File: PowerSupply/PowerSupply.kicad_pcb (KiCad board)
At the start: 2 copper layers, 34.9 x 22.9 mm, 27 parts, among them IC1 MCP73832T-2DCI_OT, J1 Conn_01x04_Male, J2 Barrel_Jack, Q1 DMP2045U-7, SW1 SW_SPST, U1 AP3012, U2 AP3012

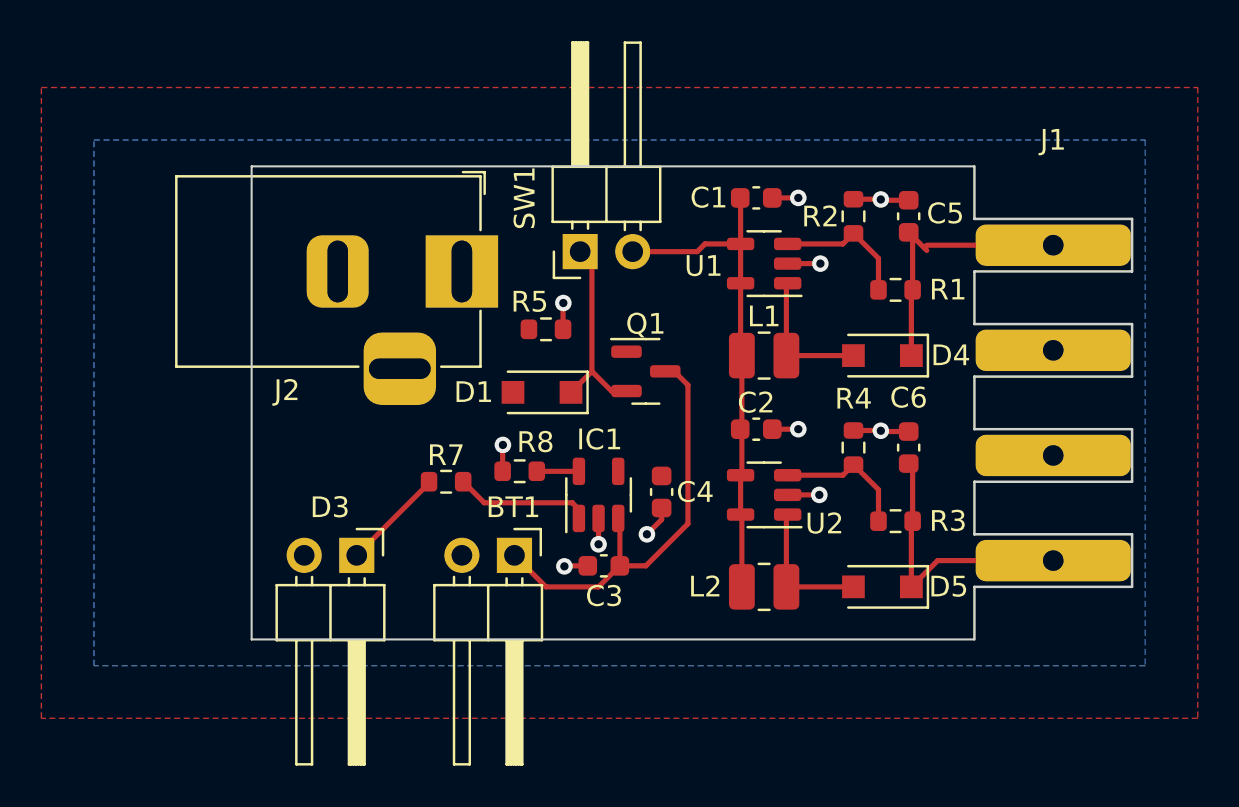
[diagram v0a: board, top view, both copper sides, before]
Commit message: Added silk screen and fabrication files.
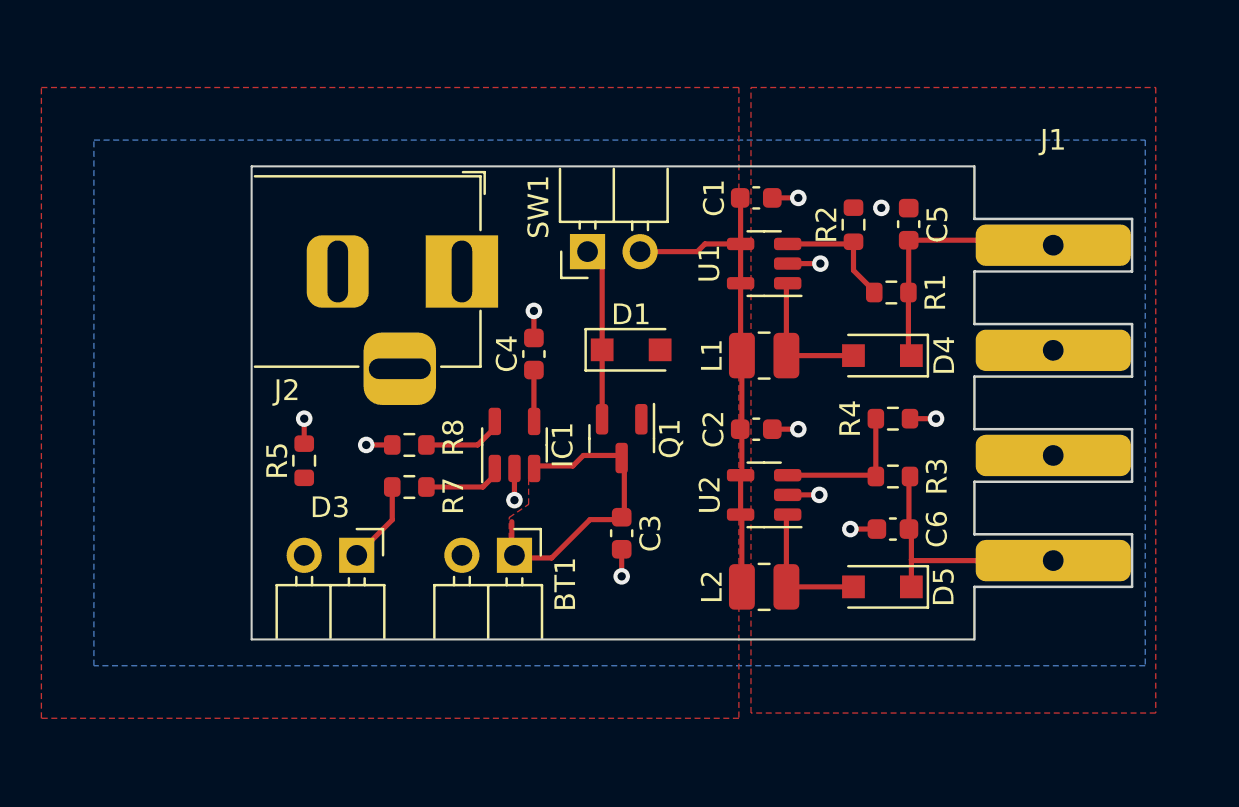
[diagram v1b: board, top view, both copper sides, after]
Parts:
- added REF**: TUNL LOGO small, Library:TUNL LOGO small, B.Cu at (167.0, 75.0)
- D1, D4, D5: value 2SS100L -> NRVB120VLSFT1G
- moved R5 13.3 mm to (142.2, 79.0), turned to 90 degrees
- moved C4 9.09 mm to (153.3, 73.8), turned to 90 degrees
- moved R8 5.48 mm to (147.3, 78.2)
- moved D1 4.77 mm to (158.0, 73.6), turned to 0 degrees
- moved IC1 4.73 mm to (152.4, 78.2)
- moved C6 4.01 mm to (170.7, 82.3), turned to 180 degrees
- moved Q1 3.45 mm to (157.6, 77.9), turned to -90 degrees
- moved R4 2.36 mm to (170.7, 77.0), turned to 0 degrees
- moved R3 2.16 mm to (170.7, 79.8)
- moved R7 1.80 mm to (147.3, 80.3)
- moved C3 1.80 mm to (157.6, 82.5), turned to 90 degrees
- moved R2 0.41 mm to (168.8, 67.6)
- moved C5 0.38 mm to (171.4, 67.6)
- moved SW1 0.36 mm to (155.9, 68.9)
- moved R1 0.24 mm to (170.6, 70.9)
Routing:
- net +BATT: track 20.7 -> 14.9 mm
- net GND: track 17.5 -> 14.8 mm, vias 11 -> 12
- net Net-(IC1-Pad1): track 6.58 -> 3.86 mm
- net +5V: track 0.00 -> 2.49 mm
- net Net-(IC1-Pad5): track 2.04 -> 3.96 mm
- net +6V: track 13.4 -> 12.3 mm
- net Net-(D1-Pad1): track 9.52 -> 8.41 mm
- net Net-(D3-Pad1): track 5.00 -> 4.01 mm
- added copper zone on F.Cu, net +BATT
- added copper zone on F.Cu, net GND
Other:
- board text added: "+24V Out"
- board text added: "+6V Out"
- board text added: "3.7V LiPo Battery"
- board text added: "5V"
- board text added: "Battery Charging LED"
- board text added: "DC in"
- board text added: "GND"
- board text added: "LED Pulser Power Board V1"
- board text added: "Output Enable"

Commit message: Optimized board and changed a few component part numbers based on availability. This version was first production board ordered.
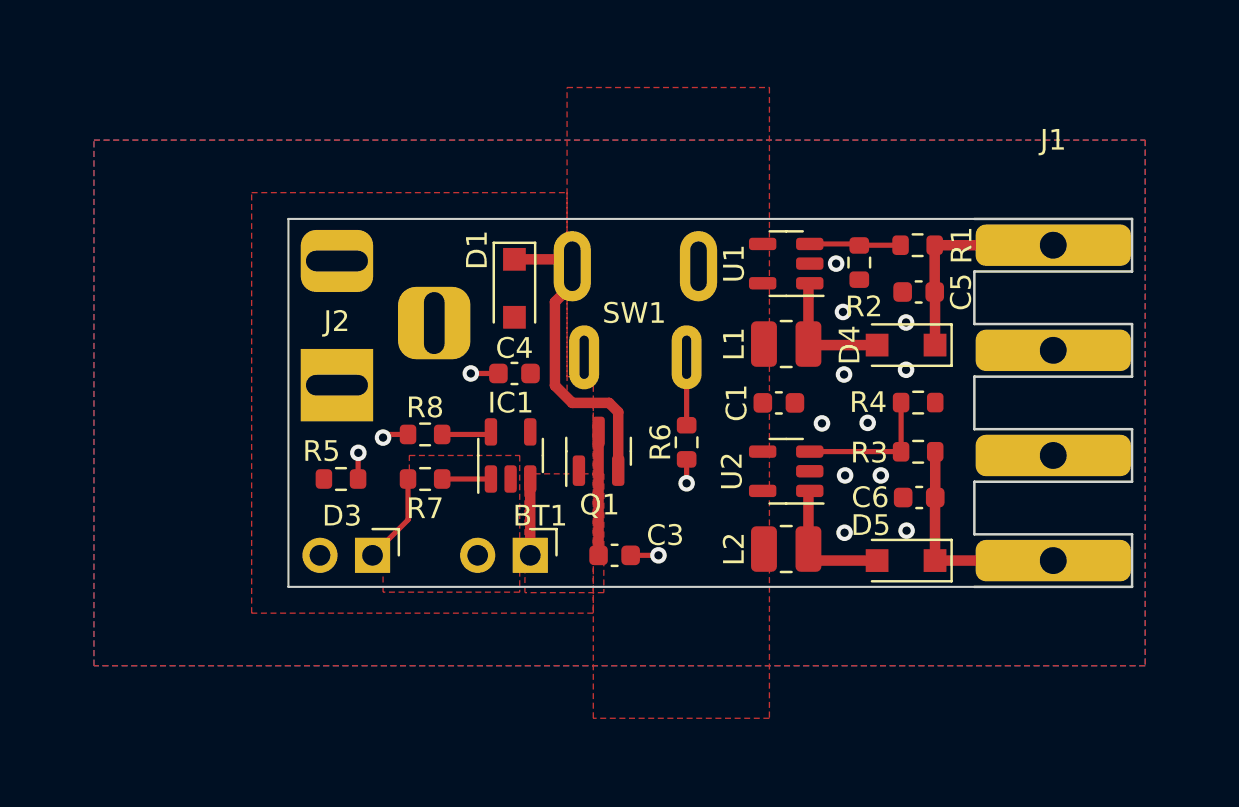
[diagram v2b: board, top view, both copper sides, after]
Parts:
- removed C2: 1uF, Capacitor_SMD:C_0603_1608Metric
- removed REF**: TUNL LOGO small, Library:TUNL LOGO small
- added LOGO1: Logo_Open_Hardware_Small, Library:TUNL LOGO OSHParkMin, B.Cu at (169.5, 77.9)
- added R6: 470, Resistor_SMD:R_0603_1608Metric, F.Cu at (160.7, 78.1)
- J2: moved to B.Cu
- SW1: value SW_SPST -> RP3508BBLKGRNGRNNS; footprint Connector_PinHeader_2.54mm:PinHeader_1x02_P2.54mm_Horizontal -> Library:RP3508x; moved to B.Cu
- moved C1 9.97 mm to (165.2, 76.2)
- moved J2 8.16 mm to (143.8, 75.3), turned to -90 degrees
- moved D1 6.37 mm to (152.4, 70.7), turned to -90 degrees
- moved C5 3.31 mm to (171.9, 70.8), turned to 180 degrees
- moved R1 2.62 mm to (171.9, 68.6)
- moved L2 2.12 mm to (165.5, 83.3)
- moved R5 1.99 mm to (144.0, 79.9), turned to 0 degrees
- moved C6 1.98 mm to (172.0, 80.8)
- moved R2 1.85 mm to (169.1, 69.4), turned to -90 degrees
- moved D5 1.71 mm to (171.3, 83.8)
- moved R3 1.71 mm to (171.9, 78.6)
- moved U2 1.56 mm to (165.5, 79.5)
- moved R4 1.45 mm to (171.9, 76.2)
- moved C4 1.33 mm to (152.4, 74.8), turned to 180 degrees
- moved Q1 1.27 mm to (156.5, 78.5), turned to 90 degrees
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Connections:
- C1 pad 1: Net-(C1-Pad1) -> VBUS
- L1 pad 1: Net-(C1-Pad1) -> VBUS
- L2 pad 1: Net-(C1-Pad1) -> VBUS
- SW1 pad 2: Net-(C1-Pad1) -> VBUS
- U1 pad 4: Net-(C1-Pad1) -> VBUS
- U1 pad 5: Net-(C1-Pad1) -> VBUS
- U2 pad 4: Net-(C1-Pad1) -> VBUS
- U2 pad 5: Net-(C1-Pad1) -> VBUS
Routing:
- net Net-(C1-Pad1): track 24.1 -> 0.00 mm
- net GND: track 14.8 -> 6.71 mm, vias 12 -> 16
- net Net-(D1-Pad1): track 8.41 -> 15.5 mm
- net +BATT: track 14.9 -> 9.66 mm
- net Net-(R6-Pad2): track 0.00 -> 3.28 mm
- net +24V: track 13.4 -> 10.6 mm
- net +5V: track 2.49 -> 0.00 mm
- net Net-(R1-Pad2): track 6.13 -> 4.42 mm
- net Net-(IC1-Pad5): track 3.96 -> 2.41 mm
- net Net-(IC1-Pad1): track 3.86 -> 2.35 mm
- net +6V: track 12.3 -> 11.0 mm
- net VBUS: track 0.00 -> 0.81 mm
- net Net-(D4-Pad2): track 6.76 -> 6.25 mm
- added copper zone on F.Cu, net VBUS
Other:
- board size 34.9 x 22.9 mm -> 33.1 x 17.8 mm
- board text added: "3.7V LiPo"
- board text added: "Charging"
- board text added: "Enable"
- board text removed: "3.7V LiPo Battery"
- board text removed: "Battery Charging LED"
- board text removed: "Output Enable"
